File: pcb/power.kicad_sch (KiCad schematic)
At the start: 2 parts, among them J1 USB_C_Receptacle, J2 USB_C_Receptacle

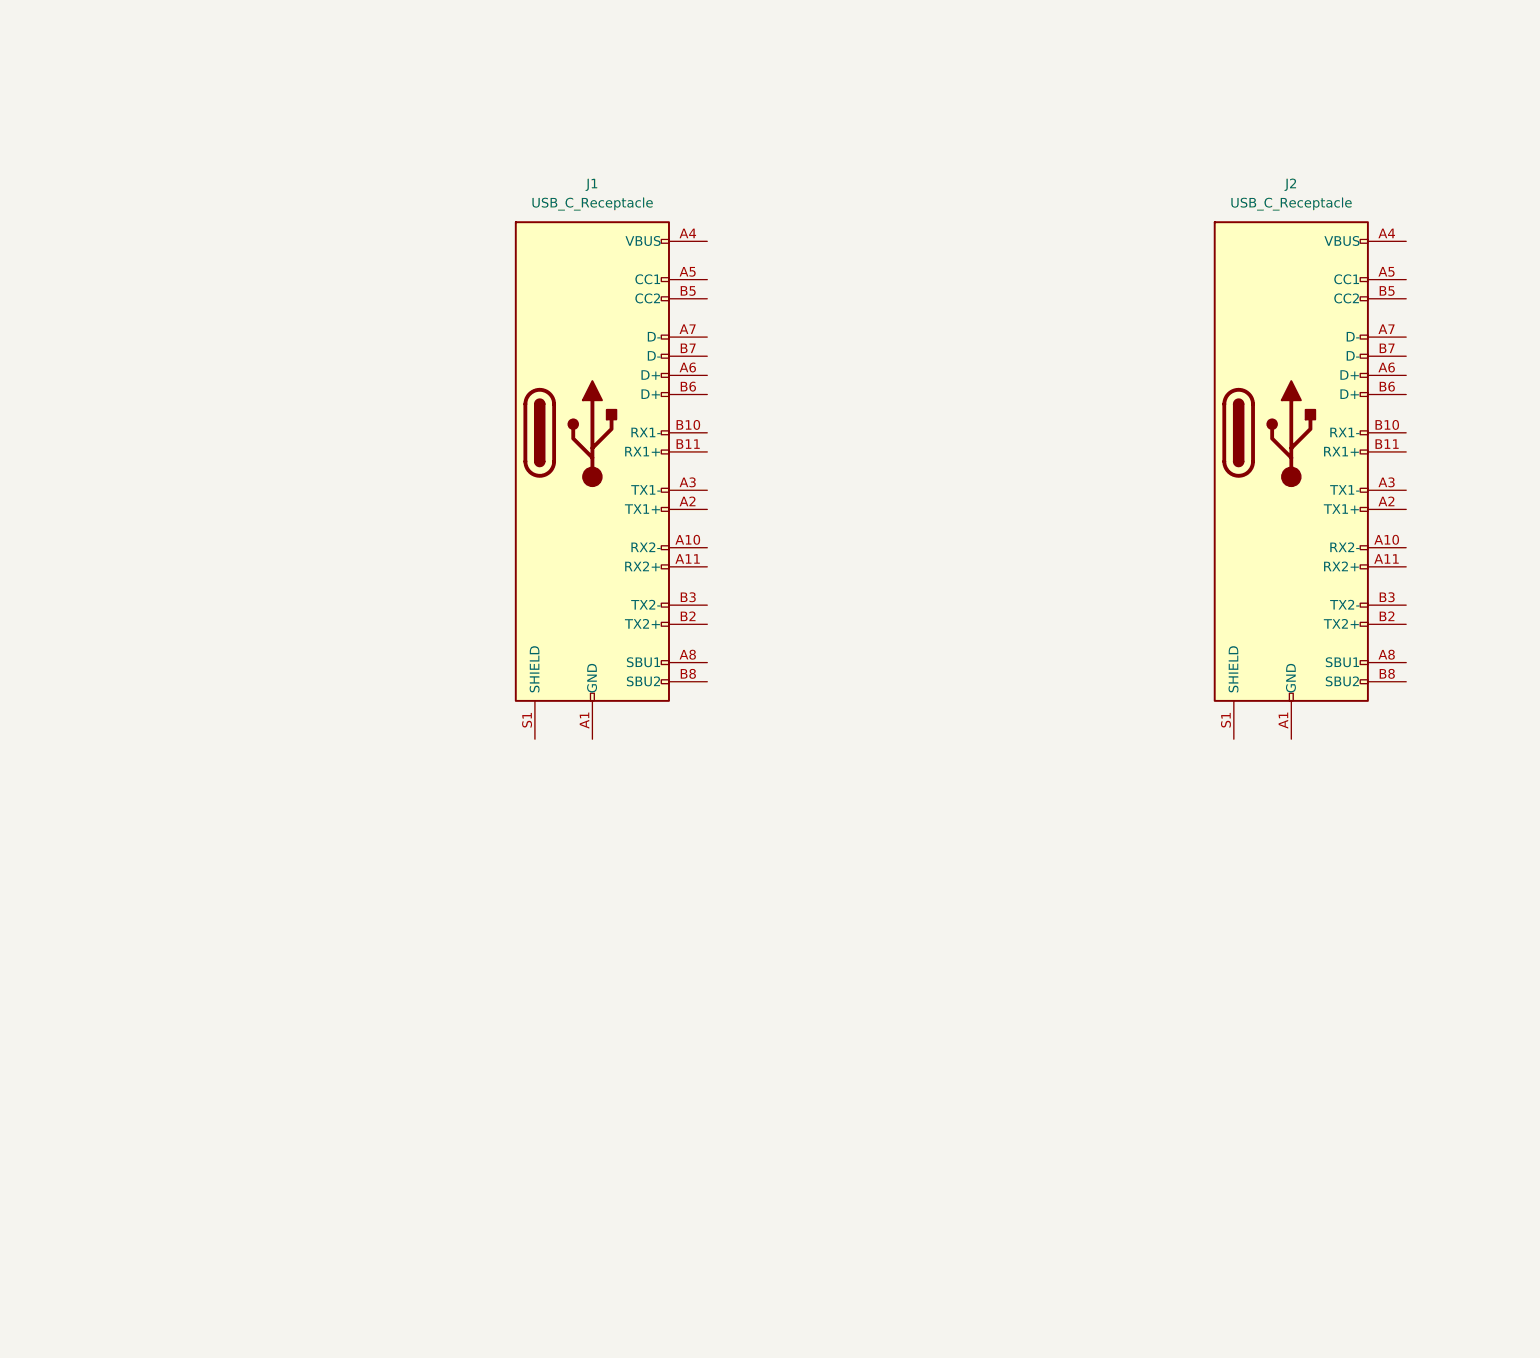
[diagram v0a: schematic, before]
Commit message: Finished most of schematic
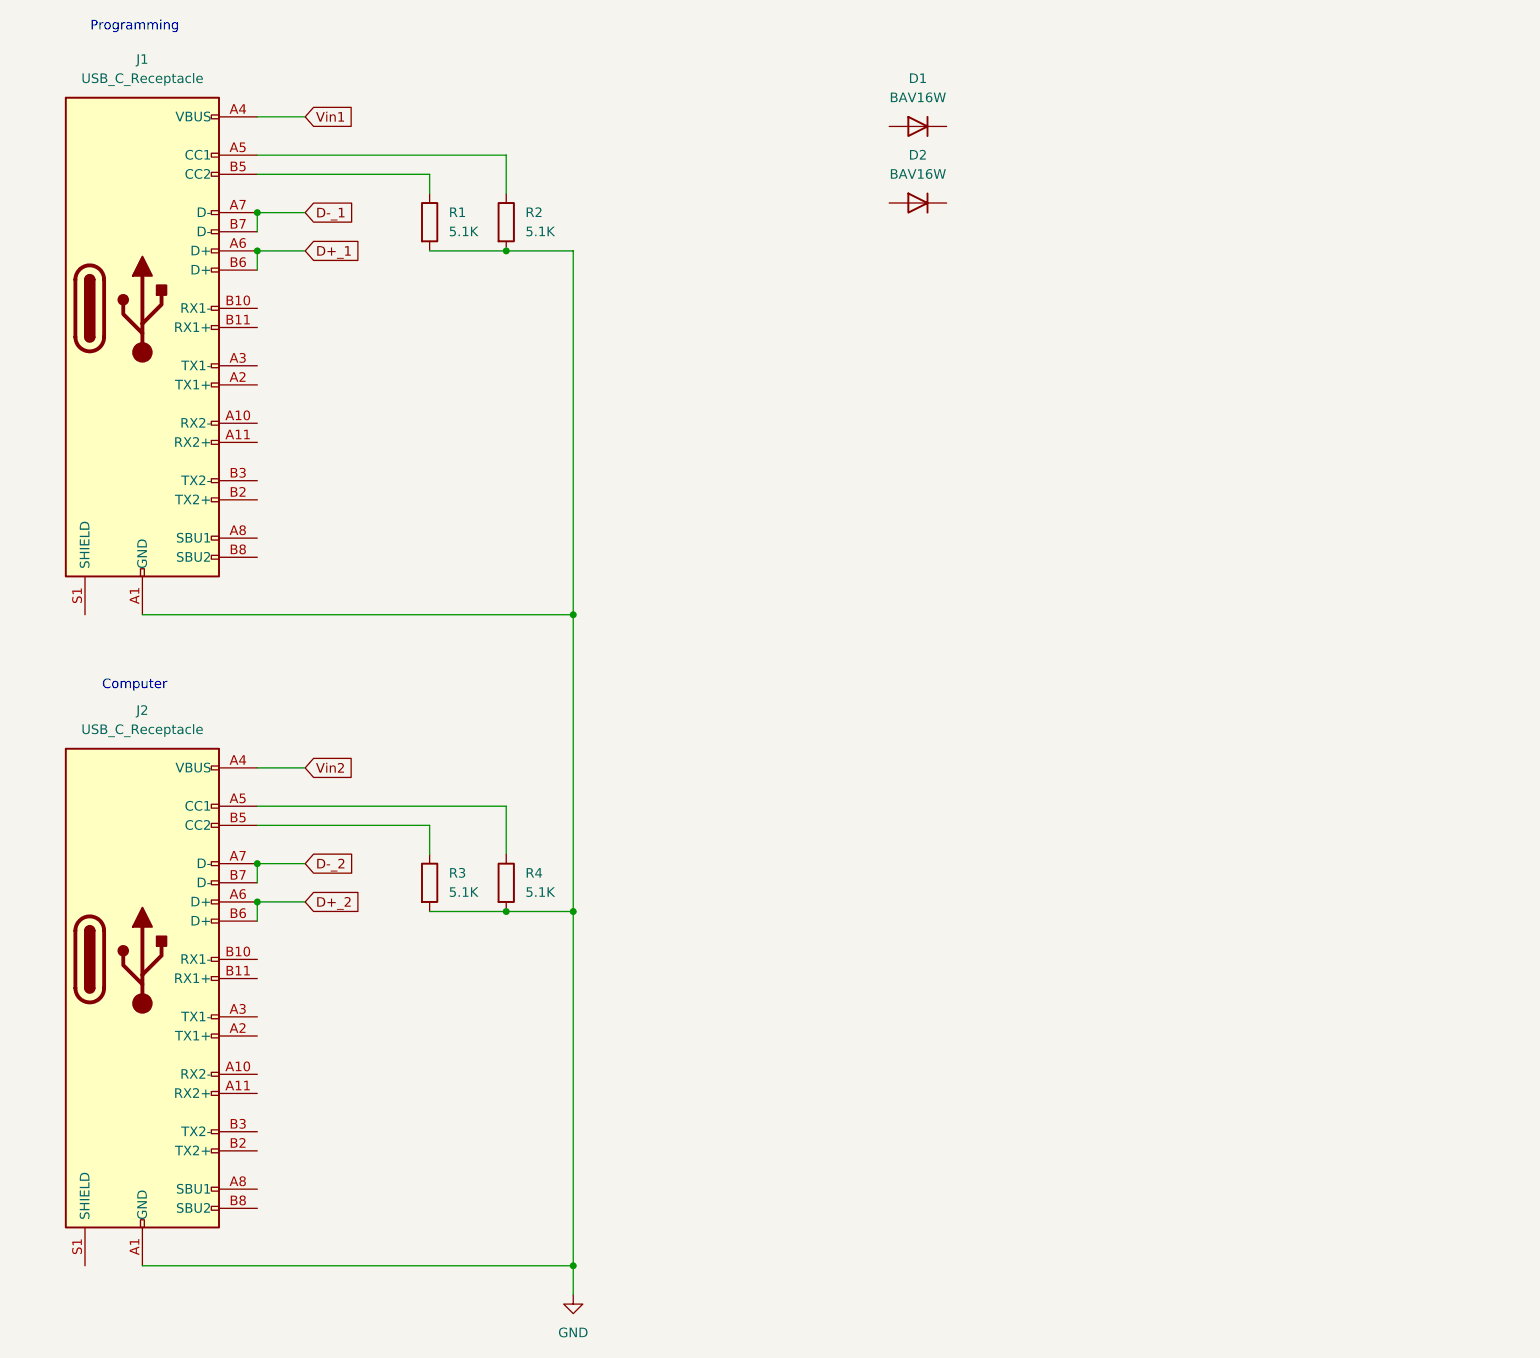
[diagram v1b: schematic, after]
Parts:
- added D1, D2: BAV16W, Diode_SMD:D_SOD-123, symbol Diode:BAV16W
- added R1, R2, R3, R4: 5.1K, Resistor_SMD:R_0402_1005Metric, symbol Device:R
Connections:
- net GND: now reaches J1.A1 (GND), J1.A12 (GND), J1.B1 (GND), J1.B12 (GND)
- net GND: now also J2.A1 (GND), J2.A12 (GND), J2.B1 (GND), J2.B12 (GND), R1.2, R2.2, R3.2, R4.2
- net Vin1: now reaches J1.A4 (VBUS), J1.A9 (VBUS), J1.B4 (VBUS), J1.B9 (VBUS)
- net at J1.A5 (CC1): now also R2.1
- net D+_1: now reaches J1.A6 (D+)
- net D+_1: now also J1.B6 (D+)
- net D-_1: now reaches J1.A7 (D-)
- net D-_1: now also J1.B7 (D-)
- net at J1.B5 (CC2): now also R1.1
- net Vin2: now reaches J2.A4 (VBUS), J2.A9 (VBUS), J2.B4 (VBUS), J2.B9 (VBUS)
- net at J2.A5 (CC1): now also R4.1
- net D+_2: now reaches J2.A6 (D+)
- net D+_2: now also J2.B6 (D+)
- net D-_2: now reaches J2.A7 (D-)
- net D-_2: now also J2.B7 (D-)
- net at J2.B5 (CC2): now also R3.1
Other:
- note added: "Computer"
- note added: "Programming"
- moved on the sheet: J1, J2

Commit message: Finished main component selection
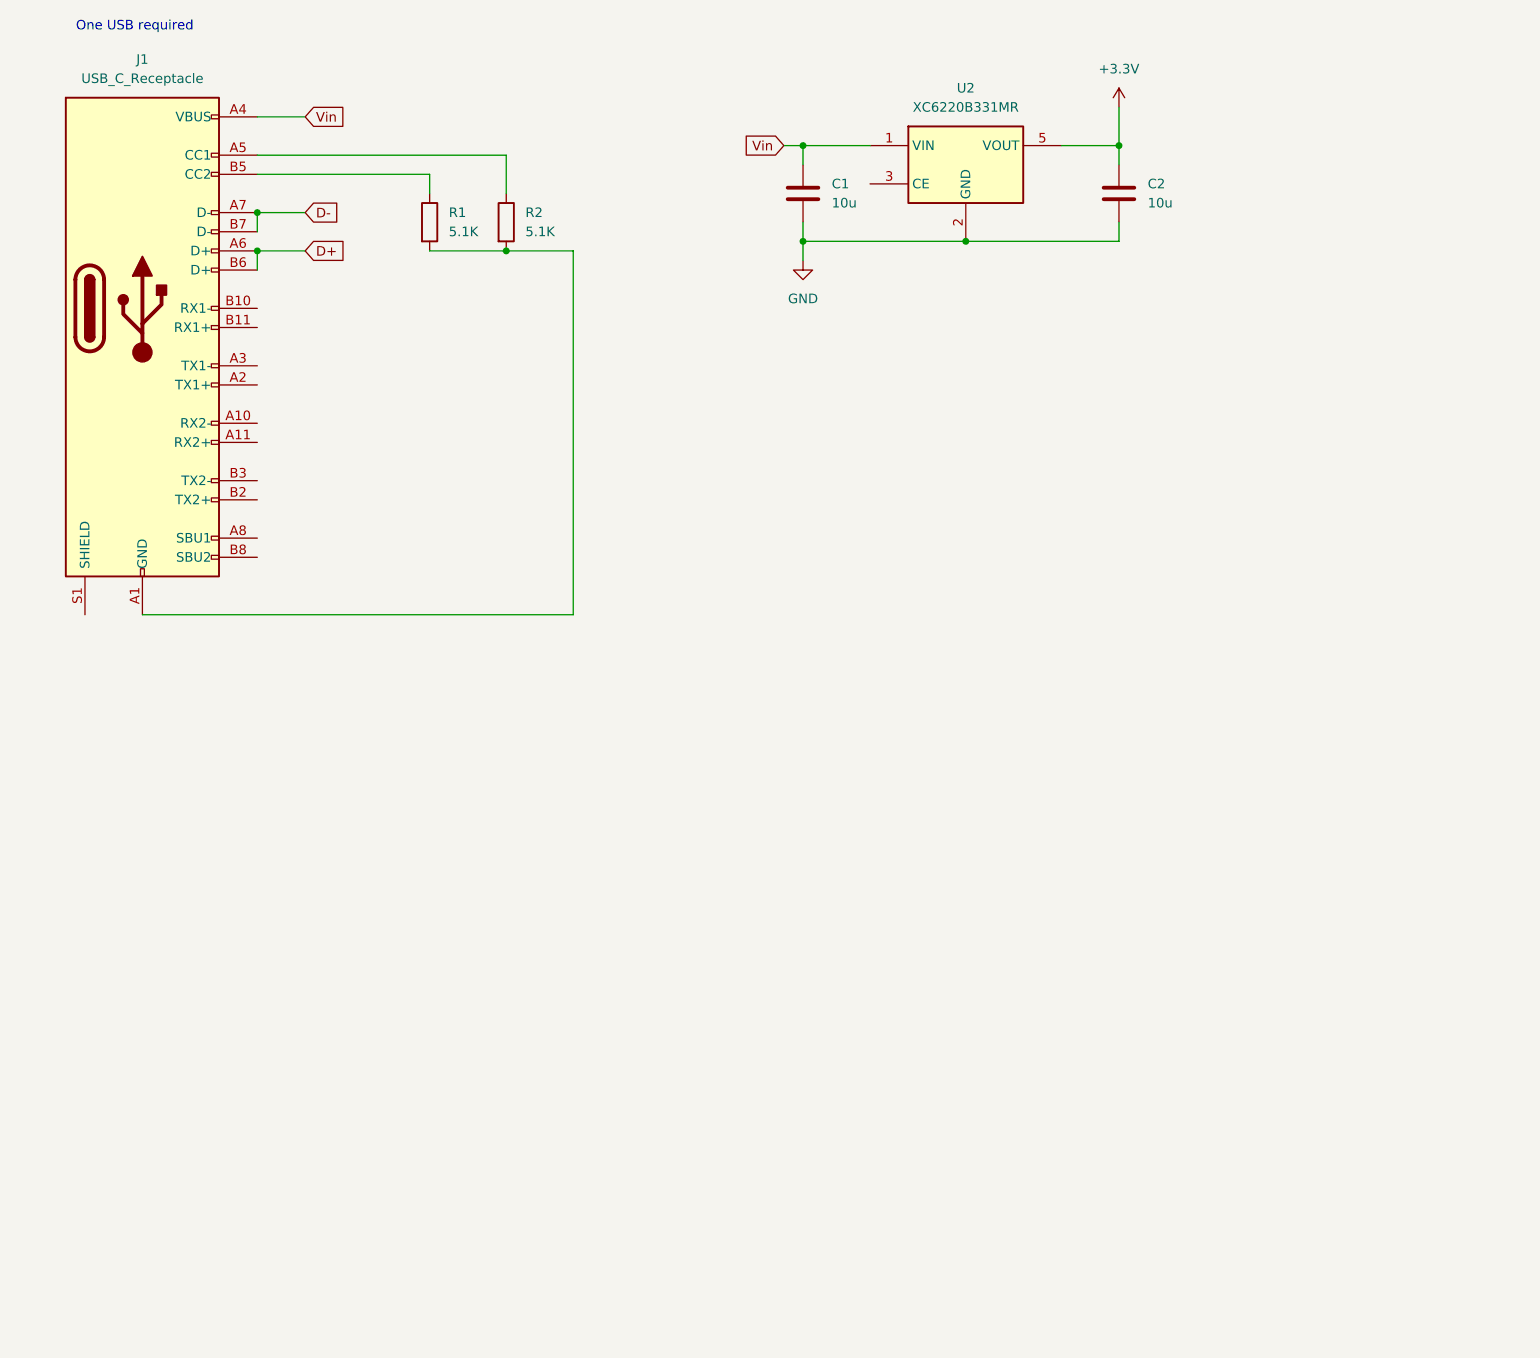
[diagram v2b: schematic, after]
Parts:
- removed D1, D2: BAV16W, Diode_SMD:D_SOD-123, symbol Diode:BAV16W
- removed J2: USB_C_Receptacle, symbol Connector:USB_C_Receptacle
- removed R3, R4: 5.1K, Resistor_SMD:R_0402_1005Metric, symbol Device:R
- added C1, C2: 10u, Capacitor_SMD:C_0402_1005Metric_Pad0.74x0.62mm_HandSolder, symbol Device:C
- added U2: XC6220B331MR, Package_TO_SOT_SMD:SOT-23-5, symbol Regulator_Linear:XC6220B331MR
- R1, R2: footprint Resistor_SMD:R_0402_1005Metric -> Resistor_SMD:R_0402_1005Metric_Pad0.72x0.64mm_HandSolder
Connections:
- net GND: now also C1.2, C2.2, U2.2 (GND); no longer J1.A1 (GND), J1.A12 (GND), J1.B1 (GND), J1.B12 (GND), R1.2, R2.2
- net D+_1 renamed D+
- net D-_1 renamed D-
- net Vin1 renamed Vin
- net Vin: now also C1.1, U2.1 (VIN)
- new net: J1.A1 (GND), J1.A12 (GND), J1.B1 (GND), J1.B12 (GND), R1.2, R2.2
- new net +3.3V: C2.1, U2.5 (VOUT)
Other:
- note added: "One USB required"
- note removed: "Computer"
- note removed: "Programming"

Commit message: All Schematic Parts Added
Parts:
- removed J1: USB_C_Receptacle, symbol Connector:USB_C_Receptacle
- added J2: USB_C_Receptacle_USB2.0_14P, Connector_USB:USB_C_Receptacle_HRO_TYPE-C-31-M-12, symbol Connector:USB_C_Receptacle_USB2.0_14P
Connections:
- net D+: now also J2.A6 (D+), J2.B6 (D+)
- net D-: now also J2.A7 (D-), J2.B7 (D-)
- net GND: now also R1.2, R2.2, J2.A1 (GND), J2.A12 (GND), J2.B1 (GND), J2.B12 (GND)
- net Vin: now also J2.A4 (VBUS), J2.A9 (VBUS), J2.B4 (VBUS), J2.B9 (VBUS)
- net at R2.1: now also J2.A5 (CC1)
- net at R1.1: now also J2.B5 (CC2)
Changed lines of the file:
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@@
+	)
+	(junction
+		(at 48.26 40.64)
+		(diameter 0)
+		(color 0 0 0 0)
 	)
 	(junction
@@
 	)
 	(junction
-		(at 48.26 40.64)
+		(at 33.02 66.04)
+		(diameter 0)
+		(color 0 0 0 0)
+	)
+	(junction
+		(at 48.26 45.72)
 		(diameter 0)
 		(color 0 0 0 0)
@@
 	)
 	(junction
-		(at 48.26 45.72)
-		(diameter 0)
-		(color 0 0 0 0)
-	)
-	(junction
 		(at 81.28 45.72)
 		(diameter 0)
@@
 	(wire
 		(pts
-			(xy 90.17 45.72) (xy 90.17 93.98)
+			(xy 90.17 45.72) (xy 90.17 66.04)
 		)
 		(stroke
@@
 	(wire
 		(pts
-			(xy 33.02 93.98) (xy 90.17 93.98)
+			(xy 33.02 66.04) (xy 90.17 66.04)
 		)
 		(stroke
@@
 	)
 	(symbol
-		(lib_id "Connector:USB_C_Receptacle")
-		(at 33.02 53.34 0)
-		(unit 1)
-		(exclude_from_sim no)
-		(in_bom yes)
-		(on_board yes)
-		(dnp no)
-		(fields_autoplaced yes)
-		(property "Reference" "J1"
-			(at 33.02 20.32 0)
-			(effects
-				(font
-					(size 1.27 1.27)
-				)
-			)
-		)
-		(property "Value" "USB_C_Receptacle"
-			(at 33.02 22.86 0)
-			(effects
-				(font
-					(size 1.27 1.27)
-				)
-			)
-		)
-		(property "Footprint" ""
-			(at 36.83 53.34 0)
-			(effects
-				(font
-					(size 1.27 1.27)
-				)
-				(hide yes)
-			)
-		)
-		(property "Datasheet" "https://www.usb.org/sites/default/files/documents/usb_type-c.zip"
-			(at 36.83 53.34 0)
-			(effects
-				(font
-					(size 1.27 1.27)
-				)
-				(hide yes)
-			)
-		)
-		(property "Description" "USB Full-Featured Type-C Receptacle connector"
-			(at 33.02 53.34 0)
-			(effects
-				(font
-					(size 1.27 1.27)
-				)
-				(hide yes)
-			)
-		)
-		(pin "B5"
-		)
-		(pin "B9"
-		)
-		(pin "A6"
-		)
-		(pin "A8"
-		)
-		(pin "A5"
-		)
-		(pin "B10"
-		)
-		(pin "A7"
-		)
-		(pin "B11"
-		)
-		(pin "A3"
-		)
-		(pin "A10"
-		)
-		(pin "A11"
-		)
-		(pin "B3"
-		)
-		(pin "B8"
-		)
-		(pin "B2"
-		)
-		(pin "A2"
-		)
-		(pin "A9"
-		)
-		(pin "B6"
-		)
-		(pin "B4"
-		)
-		(pin "B7"
-		)
-		(pin "A4"
-		)
-		(pin "B12"
-		)
-		(pin "B1"
-		)
-		(pin "A12"
-		)
-		(pin "A1"
-		)
-		(pin "S1"
-		)
-		(instances
-			(project ""
-				(path "/60f4ab9d-718b-428d-904c-5042759d3860/a1e90319-dca8-49b6-9cdf-488365fdad23"
-					(reference "J1")
-					(unit 1)
-				)
-			)
-		)
-	)
-	(symbol
 		(lib_id "Device:C")
 		(at 162.56 38.1 0)
@@
 	)
 	(symbol
+		(lib_id "power:GND")
+		(at 33.02 66.04 0)
+		(unit 1)
+		(exclude_from_sim no)
+		(in_bom yes)
+		(on_board yes)
+		(dnp no)
+		(fields_autoplaced yes)
+		(property "Reference" "#PWR012"
+			(at 33.02 72.39 0)
+			(effects
+				(font
+					(size 1.27 1.27)
+				)
+				(hide yes)
+			)
+		)
+		(property "Value" "GND"
+			(at 33.02 71.12 0)
+			(effects
+				(font
+					(size 1.27 1.27)
+				)
+			)
+		)
+		(property "Footprint" ""
+			(at 33.02 66.04 0)
+			(effects
+				(font
+					(size 1.27 1.27)
+				)
+				(hide yes)
+			)
+		)
+		(property "Datasheet" ""
+			(at 33.02 66.04 0)
+			(effects
+				(font
+					(size 1.27 1.27)
+				)
+				(hide yes)
+			)
+		)
+		(property "Description" "Power symbol creates a global label with name \"GND\" , ground"
+			(at 33.02 66.04 0)
+			(effects
+				(font
+					(size 1.27 1.27)
+				)
+				(hide yes)
+			)
+		)
+		(pin "1"
+		)
+		(instances
+			(project ""
+				(path "/60f4ab9d-718b-428d-904c-5042759d3860/a1e90319-dca8-49b6-9cdf-488365fdad23"
+					(reference "#PWR012")
+					(unit 1)
+				)
+			)
+		)
+	)
+	(symbol
 		(lib_id "Device:C")
 		(at 120.65 38.1 0)
@@
 					(unit 1)
 				)
+			)
+		)
+	)
+	(symbol
+		(lib_id "Connector:USB_C_Receptacle_USB2.0_14P")
+		(at 33.02 43.18 0)
+		(unit 1)
+		(exclude_from_sim no)
+		(in_bom yes)
+		(on_board yes)
+		(dnp no)
+		(fields_autoplaced yes)
+		(property "Reference" "J2"
+			(at 33.02 20.32 0)
+			(effects
+				(font
+					(size 1.27 1.27)
+				)
+			)
+		)
+		(property "Value" "USB_C_Receptacle_USB2.0_14P"
+			(at 33.02 22.86 0)
+			(effects
+				(font
+					(size 1.27 1.27)
+				)
+			)
+		)
+		(property "Footprint" "Connector_USB:USB_C_Receptacle_HRO_TYPE-C-31-M-12"
+			(at 36.83 43.18 0)
+			(effects
+				(font
+					(size 1.27 1.27)
+				)
+				(hide yes)
+			)
+		)
+		(property "Datasheet" "https://www.usb.org/sites/default/files/documents/usb_type-c.zip"
+			(at 36.83 43.18 0)
+			(effects
+				(font
+					(size 1.27 1.27)
+				)
+				(hide yes)
+			)
+		)
+		(property "Description" "USB 2.0-only 14P Type-C Receptacle connector"
+			(at 33.02 43.18 0)
+			(effects
+				(font
+					(size 1.27 1.27)
+				)
+				(hide yes)
+			)
+		)
+		(pin "A7"
+		)
+		(pin "A5"
+		)
+		(pin "A1"
+		)
+		(pin "S1"
+		)
+		(pin "A4"
+		)
+		(pin "B7"
+		)
+		(pin "B1"
+		)
+		(pin "A12"
+		)
+		(pin "A9"
+		)
+		(pin "B9"
+		)
+		(pin "B6"
+		)
+		(pin "B5"
+		)
+		(pin "B12"
+		)
+		(pin "A6"
+		)
+		(pin "B4"
+		)
+		(instances
+			(project ""
+				(path "/60f4ab9d-718b-428d-904c-5042759d3860/a1e90319-dca8-49b6-9cdf-488365fdad23"
+					(reference "J2")
+					(unit 1)
+				)

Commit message: Schematic finalized and general layout completed
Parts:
- added D1, D2, D3, D4, D5: D_TVS, Diode_SMD:D_SOD-123, symbol Device:D_TVS
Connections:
- net D+: now also D4.1 (A1)
- net D-: now also D5.1 (A1)
- net GND: now also D1.2 (A2), D2.2 (A2), D3.2 (A2), D4.2 (A2), D5.2 (A2)
- net Vin: now also D1.1 (A1)
- net at J2.B5 (CC2), R1.1: now also D3.1 (A1)
- net at J2.A5 (CC1), R2.1: now also D2.1 (A1)
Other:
- moved on the sheet: C1, C2, R1, R2, U2

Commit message: Finished board, with maybe some cleanup needed
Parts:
- removed D2, D3: D_TVS, Diode_SMD:D_SOD-123, symbol Device:D_TVS
- removed J2: USB_C_Receptacle_USB2.0_14P, Connector_USB:USB_C_Receptacle_HRO_TYPE-C-31-M-12, symbol Connector:USB_C_Receptacle_USB2.0_14P
- added J1: USB_C_Receptacle_USB2.0_16P, Connector_USB:USB_C_Receptacle_HRO_TYPE-C-31-M-12, symbol Connector:USB_C_Receptacle_USB2.0_16P
- D1, D4, D5: footprint Diode_SMD:D_SOD-123 -> Diode_SMD:D_SOD-323_HandSoldering
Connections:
- net D+: now also J1.A6 (D+), J1.B6 (D+)
- net D-: now also J1.A7 (D-), J1.B7 (D-)
- net GND: now also J1.A1 (GND), J1.A12 (GND), J1.B1 (GND), J1.B12 (GND)
- net Vin: now also J1.A4 (VBUS), J1.A9 (VBUS), J1.B4 (VBUS), J1.B9 (VBUS)
- net at R2.1: now also J1.A5 (CC1)
- net at R1.1: now also J1.B5 (CC2)
